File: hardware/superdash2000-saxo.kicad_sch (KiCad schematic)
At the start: 21 parts, among them IC1 MAX4617CPE+, J1 Molex 34691-0161, U1 L7805, U2 TLV2372

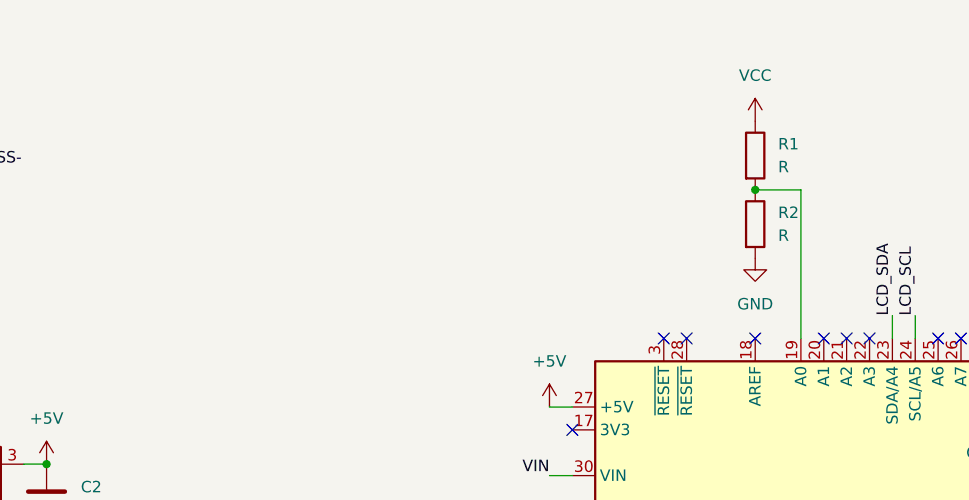
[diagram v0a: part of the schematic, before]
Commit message: hardware: Split bat voltage divider and mcu
Signed-off-by: Thomas Antonini <antonini.thomas@gmail.com>
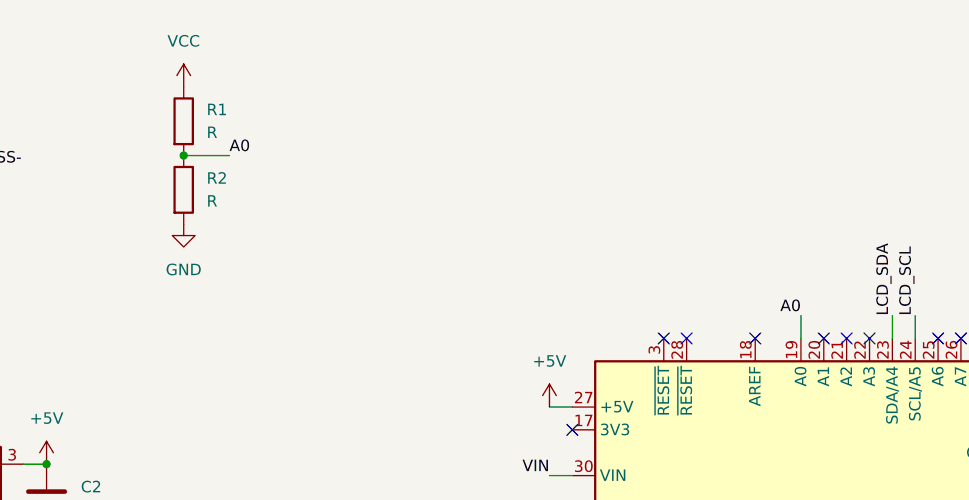
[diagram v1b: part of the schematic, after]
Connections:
- net A0: now reaches A1.19 (A0), R1.2, R2.1
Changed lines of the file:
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@@
   (junction (at 73.66 105.41) (diameter 0) (color 0 0 0 0)
   )
+  (junction (at 91.44 30.48) (diameter 0) (color 0 0 0 0)
+  )
   (junction (at 34.29 71.12) (diameter 0) (color 0 0 0 0)
-  )
-  (junction (at 154.94 34.29) (diameter 0) (color 0 0 0 0)
   )
   (junction (at 66.04 72.39) (diameter 0) (color 0 0 0 0)
@@
     (stroke (width 0) (type default) (color 0 0 0 0))
   )
+  (wire (pts (xy 160.02 48.26) (xy 160.02 50.8))
+    (stroke (width 0) (type default) (color 0 0 0 0))
+  )
   (wire (pts (xy 119.38 105.41) (xy 128.27 105.41))
     (stroke (width 0) (type default) (color 0 0 0 0))
@@
     (stroke (width 0) (type default) (color 0 0 0 0))
   )
-  (wire (pts (xy 160.02 34.29) (xy 154.94 34.29))
-    (stroke (width 0) (type default) (color 0 0 0 0))
-  )
   (wire (pts (xy 237.49 129.54) (xy 237.49 127))
     (stroke (width 0) (type default) (color 0 0 0 0))
@@
     (stroke (width 0) (type default) (color 0 0 0 0))
   )
-  (wire (pts (xy 160.02 50.8) (xy 160.02 34.29))
-    (stroke (width 0) (type default) (color 0 0 0 0))
-  )
   (wire (pts (xy 34.29 24.13) (xy 34.29 26.67))
     (stroke (width 0) (type default) (color 0 0 0 0))
@@
     (stroke (width 0) (type default) (color 0 0 0 0))
   )
+  (wire (pts (xy 96.52 30.48) (xy 91.44 30.48))
+    (stroke (width 0) (type default) (color 0 0 0 0))
+  )
   (wire (pts (xy 119.38 111.76) (xy 119.38 105.41))
     (stroke (width 0) (type default) (color 0 0 0 0))
@@
     (effects (font (size 1.27 1.27)) (justify right bottom))
   )
+  (label "A0" (at 96.52 30.48 0)
+    (effects (font (size 1.27 1.27)) (justify left bottom))
+  )
   (label "BUTTON+" (at 57.15 34.29 0)
     (effects (font (size 1.27 1.27)) (justify left bottom))
@@
     (effects (font (size 1.27 1.27)) (justify left bottom))
   )
+  (label "A0" (at 160.02 48.26 180)
+    (effects (font (size 1.27 1.27)) (justify right bottom))
+  )
   (label "LCD_SCL" (at 172.72 48.26 90)
     (effects (font (size 1.27 1.27)) (justify left bottom))
@@
   (label "+5V" (at 228.6 119.38 0)
     (effects (font (size 1.27 1.27)) (justify left bottom))
+  )
+  (symbol (lib_id "Device:R") (at 91.44 34.29 0) (unit 1)
+    (in_bom yes) (on_board yes) (fields_autoplaced)
+    (property "Reference" "R2" (id 0) (at 93.98 33.0199 0)
+      (effects (font (size 1.27 1.27)) (justify left))
+    )
+    (property "Value" "R" (id 1) (at 93.98 35.5599 0)
+      (effects (font (size 1.27 1.27)) (justify left))
+    )
+    (property "Footprint" "" (id 2) (at 89.662 34.29 90)
+      (effects (font (size 1.27 1.27)) hide)
+    )
+    (property "Datasheet" "~" (id 3) (at 91.44 34.29 0)
+      (effects (font (size 1.27 1.27)) hide)
+    )
+    (pin "1")
+    (pin "2")
   )
   (symbol (lib_id "Device:R_Potentiometer") (at 245.11 139.7 90) (unit 1)
@@
     (pin "3")
   )
+  (symbol (lib_id "power:VCC") (at 91.44 22.86 0) (unit 1)
+    (in_bom yes) (on_board yes) (fields_autoplaced)
+    (property "Reference" "#PWR06" (id 0) (at 91.44 26.67 0)
+      (effects (font (size 1.27 1.27)) hide)
+    )
+    (property "Value" "VCC" (id 1) (at 91.44 17.78 0))
+    (property "Footprint" "" (id 2) (at 91.44 22.86 0)
+      (effects (font (size 1.27 1.27)) hide)
+    )
+    (property "Datasheet" "" (id 3) (at 91.44 22.86 0)
+      (effects (font (size 1.27 1.27)) hide)
+    )
+    (pin "1")
+  )
   (symbol (lib_id "power:GND") (at 185.42 63.5 0) (unit 1)
     (in_bom yes) (on_board yes) (fields_autoplaced)
@@
     (pin "1")
   )
-  (symbol (lib_id "power:VCC") (at 154.94 26.67 0) (unit 1)
-    (in_bom yes) (on_board yes) (fields_autoplaced)
-    (property "Reference" "#PWR011" (id 0) (at 154.94 30.48 0)
-      (effects (font (size 1.27 1.27)) hide)
-    )
-    (property "Value" "VCC" (id 1) (at 154.94 21.59 0))
-    (property "Footprint" "" (id 2) (at 154.94 26.67 0)
-      (effects (font (size 1.27 1.27)) hide)
-    )
-    (property "Datasheet" "" (id 3) (at 154.94 26.67 0)
-      (effects (font (size 1.27 1.27)) hide)
-    )
-    (pin "1")
-  )
   (symbol (lib_id "power:GND") (at 34.29 24.13 270) (unit 1)
     (in_bom yes) (on_board yes) (fields_autoplaced)
@@
     )
     (property "Datasheet" "" (id 3) (at 34.29 24.13 0)
-      (effects (font (size 1.27 1.27)) hide)
-    )
-    (pin "1")
-  )
-  (symbol (lib_name "GND_1") (lib_id "power:GND") (at 154.94 41.91 0) (unit 1)
-    (in_bom yes) (on_board yes) (fields_autoplaced)
-    (property "Reference" "#PWR06" (id 0) (at 154.94 48.26 0)
-      (effects (font (size 1.27 1.27)) hide)
-    )
-    (property "Value" "GND" (id 1) (at 154.94 46.99 0))
-    (property "Footprint" "" (id 2) (at 154.94 41.91 0)
-      (effects (font (size 1.27 1.27)) hide)
-    )
-    (property "Datasheet" "" (id 3) (at 154.94 41.91 0)
       (effects (font (size 1.27 1.27)) hide)
     )
@@
     (pin "2")
   )
+  (symbol (lib_id "Device:R") (at 91.44 26.67 0) (unit 1)
+    (in_bom yes) (on_board yes) (fields_autoplaced)
+    (property "Reference" "R1" (id 0) (at 93.98 25.3999 0)
+      (effects (font (size 1.27 1.27)) (justify left))
+    )
+    (property "Value" "R" (id 1) (at 93.98 27.9399 0)
+      (effects (font (size 1.27 1.27)) (justify left))
+    )
+    (property "Footprint" "" (id 2) (at 89.662 26.67 90)
+      (effects (font (size 1.27 1.27)) hide)
+    )
+    (property "Datasheet" "~" (id 3) (at 91.44 26.67 0)
+      (effects (font (size 1.27 1.27)) hide)
+    )
+    (pin "1")
+    (pin "2")
+  )
   (symbol (lib_id "Molex_34691-0161:Molex 34691-0161") (at 34.29 24.13 0) (unit 1)
     (in_bom yes) (on_board yes) (fields_autoplaced)
@@
     (pin "1")
   )
+  (symbol (lib_name "GND_1") (lib_id "power:GND") (at 91.44 38.1 0) (unit 1)
+    (in_bom yes) (on_board yes) (fields_autoplaced)
+    (property "Reference" "#PWR011" (id 0) (at 91.44 44.45 0)
+      (effects (font (size 1.27 1.27)) hide)
+    )
+    (property "Value" "GND" (id 1) (at 91.44 43.18 0))
+    (property "Footprint" "" (id 2) (at 91.44 38.1 0)
+      (effects (font (size 1.27 1.27)) hide)
+    )
+    (property "Datasheet" "" (id 3) (at 91.44 38.1 0)
+      (effects (font (size 1.27 1.27)) hide)
+    )
+    (pin "1")
+  )
   (symbol (lib_id "power:+5V") (at 57.15 26.67 270) (unit 1)
     (in_bom yes) (on_board yes) (fields_autoplaced)
@@
     (pin "2")
   )
-  (symbol (lib_id "Device:R") (at 154.94 30.48 0) (unit 1)
-    (in_bom yes) (on_board yes) (fields_autoplaced)
-    (property "Reference" "R1" (id 0) (at 157.48 29.2099 0)
-      (effects (font (size 1.27 1.27)) (justify left))
-    )
-    (property "Value" "R" (id 1) (at 157.48 31.7499 0)
-      (effects (font (size 1.27 1.27)) (justify left))
-    )
-    (property "Footprint" "" (id 2) (at 153.162 30.48 90)
-      (effects (font (size 1.27 1.27)) hide)
-    )
-    (property "Datasheet" "~" (id 3) (at 154.94 30.48 0)
-      (effects (font (size 1.27 1.27)) hide)
-    )
-    (pin "1")
-    (pin "2")
-  )
-  (symbol (lib_id "Device:R") (at 154.94 38.1 0) (unit 1)
-    (in_bom yes) (on_board yes) (fields_autoplaced)
-    (property "Reference" "R2" (id 0) (at 157.48 36.8299 0)
-      (effects (font (size 1.27 1.27)) (justify left))
-    )
-    (property "Value" "R" (id 1) (at 157.48 39.3699 0)
-      (effects (font (size 1.27 1.27)) (justify left))
-    )
-    (property "Footprint" "" (id 2) (at 153.162 38.1 90)
-      (effects (font (size 1.27 1.27)) hide)
-    )
-    (property "Datasheet" "~" (id 3) (at 154.94 38.1 0)
-      (effects (font (size 1.27 1.27)) hide)
-    )
-    (pin "1")
-    (pin "2")
-  )
   (sheet_instances
     (path "/" (page "1"))
@@
       (reference "#PWR05") (unit 1) (value "GND") (footprint "")
     )
-    (path "/2c2c0160-d229-41a2-b822-4cf1420ec8e9"
-      (reference "#PWR06") (unit 1) (value "GND") (footprint "")
+    (path "/084d9e07-e47a-4b4b-9d62-a6a579a1f476"
+      (reference "#PWR06") (unit 1) (value "VCC") (footprint "")
     )
     (path "/7c43fb8d-99fb-43c3-9bcb-9181569a93c6"
@@
       (reference "#PWR010") (unit 1) (value "VCC") (footprint "")
     )
-    (path "/19afe61c-2254-4882-aed9-fe6a1372b102"
-      (reference "#PWR011") (unit 1) (value "VCC") (footprint "")
+    (path "/c9b9529e-a50b-4a27-8db1-29bd22c717fc"
+      (reference "#PWR011") (unit 1) (value "GND") (footprint "")
     )
     (path "/b753003b-957e-4f15-9660-b86b3ddd77f6"
@@
       (reference "JP1") (unit 1) (value "Jumper_3_Bridged12") (footprint "")
     )
-    (path "/f89ebb12-89cc-4956-9979-cdeb115f9256"
+    (path "/76311df4-9ae4-417e-9a2a-a08c856f4678"
       (reference "R1") (unit 1) (value "R") (footprint "")
     )
-    (path "/fece9861-2ca2-4e20-aacd-7057d18618e8"
+    (path "/005dc53c-66e1-42ad-99cb-f5a004950864"
       (reference "R2") (unit 1) (value "R") (footprint "")
     )

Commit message: hardware: Update footprints
Signed-off-by: Thomas Antonini <antonini.thomas@gmail.com>
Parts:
- C1, C2: footprint Capacitor_THT:C_Disc_D3.0mm_W1.6mm_P2.50mm -> Capacitor_THT:C_Disc_D5.0mm_W2.5mm_P2.50mm
- C3: footprint (none) -> Capacitor_THT:C_Disc_D5.0mm_W2.5mm_P2.50mm
- IC1: footprint DIP794W56P254L1918H457Q16N -> Package_DIP:DIP-16_W7.62mm
- JP1: footprint (none) -> Connector_PinHeader_2.54mm:PinHeader_1x03_P2.54mm_Vertical
- R1, R2, R3, R4, R5, R6, R7, R8, R9: footprint (none) -> Resistor_THT:R_Axial_DIN0207_L6.3mm_D2.5mm_P7.62mm_Horizontal
- RV1, RV2: footprint (none) -> Potentiometer_THT:Potentiometer_Bourns_3296W_Vertical
- U2: footprint (none) -> Package_DIP:DIP-8_W7.62mm

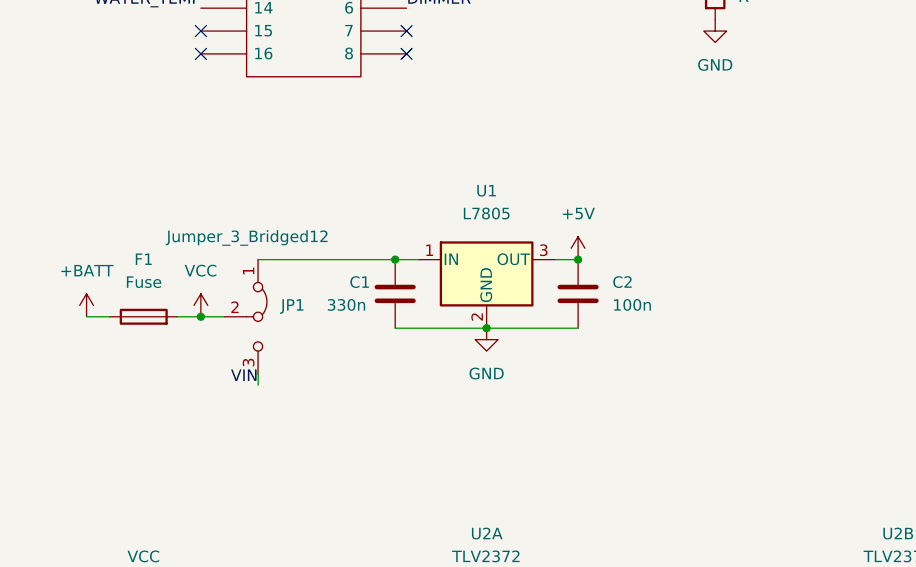
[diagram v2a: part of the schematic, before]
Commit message: hardware: Modify fuse with one added in lib
Signed-off-by: Thomas Antonini <antonini.thomas@gmail.com>
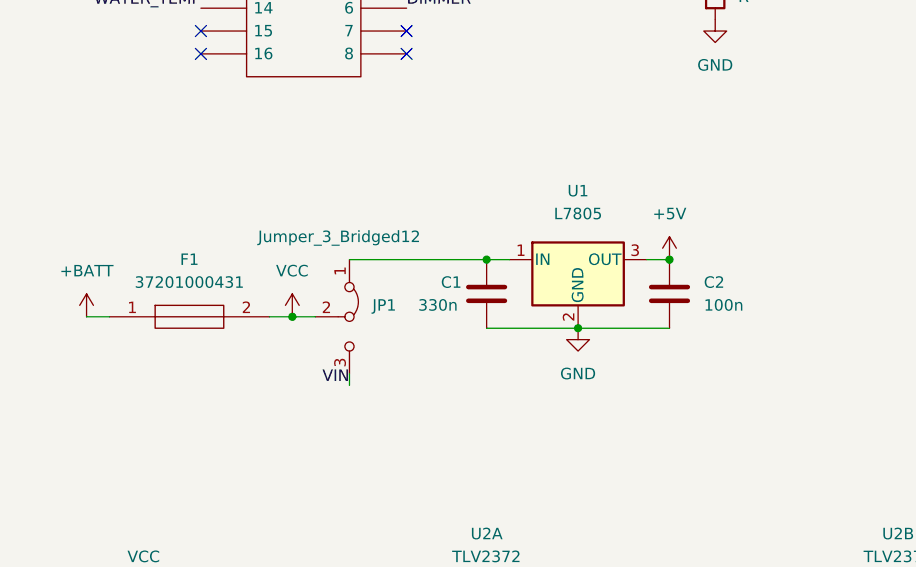
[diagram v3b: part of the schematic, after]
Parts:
- removed F1: Fuse, symbol Device:Fuse
- added F1: 37201000431, Littlefuse_37201000431:37201000431, symbol Littlefuse_37201000431:37201000431
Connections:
- net +BATT: now also F1.1
- net VCC: now also F1.2
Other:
- moved on the sheet: C1, C2, JP1, U1

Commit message: hardware: Update arduino footprint
Signed-off-by: Thomas Antonini <antonini.thomas@gmail.com>
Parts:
- A1: footprint Module:Arduino_Nano -> Arduino_Nano_Every:Arduino_Nano_Every_WithMountingHoles
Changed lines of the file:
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@@
     (property "Reference" "A1" (id 0) (at 194.31 59.9186 90))
     (property "Value" "Arduino_Nano_Every" (id 1) (at 194.31 62.4586 90))
-    (property "Footprint" "Module:Arduino_Nano" (id 2) (at 160.02 63.5 0)
+    (property "Footprint" "Arduino_Nano_Every:Arduino_Nano_Every_WithMountingHoles" (id 2) (at 160.02 63.5 0)
       (effects (font (size 1.27 1.27) italic) hide)
     )
@@
     )
     (path "/65c02b6a-4170-4a63-9193-eec01920d5e8"
-      (reference "A1") (unit 1) (value "Arduino_Nano_Every") (footprint "Module:Arduino_Nano")
+      (reference "A1") (unit 1) (value "Arduino_Nano_Every") (footprint "Arduino_Nano_Every:Arduino_Nano_Every_WithMountingHoles")
     )
     (path "/eae34f3b-9c4a-4c30-981e-9737d2460a8b"

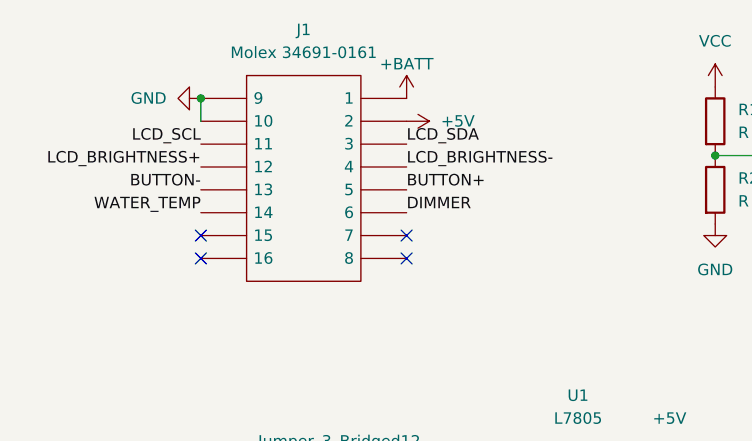
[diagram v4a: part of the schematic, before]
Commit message: hardware: Invert LCD_BRIGHTNESS+/-
Signed-off-by: Thomas Antonini <antonini.thomas@gmail.com>
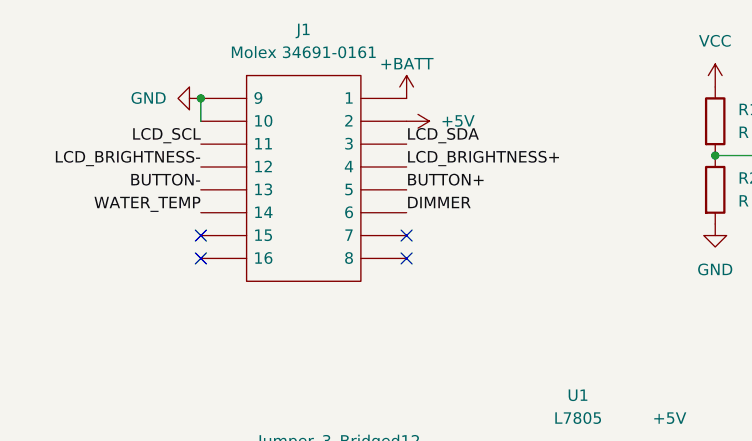
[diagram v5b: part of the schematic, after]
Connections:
- net LCD_BRIGHTNESS+: now also J1.4; no longer J1.12
- net LCD_BRIGHTNESS-: now also J1.12; no longer J1.4
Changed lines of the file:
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@@
     (effects (font (size 1.27 1.27)) (justify right bottom))
   )
-  (label "LCD_BRIGHTNESS+" (at 34.29 31.75 180)
+  (label "LCD_BRIGHTNESS-" (at 34.29 31.75 180)
     (effects (font (size 1.27 1.27)) (justify right bottom))
   )
@@
     (effects (font (size 1.27 1.27)) (justify right bottom))
   )
-  (label "LCD_BRIGHTNESS-" (at 57.15 31.75 0)
+  (label "LCD_BRIGHTNESS+" (at 57.15 31.75 0)
     (effects (font (size 1.27 1.27)) (justify left bottom))
   )

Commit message: hardware: Change arduino footprint to without holes
Signed-off-by: Thomas Antonini <antonini.thomas@gmail.com>
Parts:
- A1: footprint Arduino_Nano_Every:Arduino_Nano_Every_WithMountingHoles -> Arduino_Nano_Every:Arduino_Nano_Every
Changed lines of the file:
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@@
     (property "Reference" "A1" (id 0) (at 194.31 59.9186 90))
     (property "Value" "Arduino_Nano_Every" (id 1) (at 194.31 62.4586 90))
-    (property "Footprint" "Arduino_Nano_Every:Arduino_Nano_Every_WithMountingHoles" (id 2) (at 160.02 63.5 0)
+    (property "Footprint" "Arduino_Nano_Every:Arduino_Nano_Every" (id 2) (at 160.02 63.5 0)
       (effects (font (size 1.27 1.27) italic) hide)
     )
@@
     )
     (path "/65c02b6a-4170-4a63-9193-eec01920d5e8"
-      (reference "A1") (unit 1) (value "Arduino_Nano_Every") (footprint "Arduino_Nano_Every:Arduino_Nano_Every_WithMountingHoles")
+      (reference "A1") (unit 1) (value "Arduino_Nano_Every") (footprint "Arduino_Nano_Every:Arduino_Nano_Every")
     )
     (path "/eae34f3b-9c4a-4c30-981e-9737d2460a8b"

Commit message: hardare: Update pcb
Signed-off-by: Thomas Antonini <antonini.thomas@gmail.com>
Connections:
- net D3: now also R7.2, R8.1; no longer R3.2, R4.2
- net D4: now also R3.2, R4.2; no longer R7.2, R8.1
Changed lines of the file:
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@@
     (effects (font (size 1.27 1.27)) (justify left bottom))
   )
-  (label "D4" (at 129.54 114.3 0)
+  (label "D3" (at 129.54 114.3 0)
     (effects (font (size 1.27 1.27)) (justify left bottom))
   )
@@
     (effects (font (size 1.27 1.27)) (justify left bottom))
   )
-  (label "D3" (at 83.82 114.3 0)
+  (label "D4" (at 83.82 114.3 0)
     (effects (font (size 1.27 1.27)) (justify left bottom))
   )
